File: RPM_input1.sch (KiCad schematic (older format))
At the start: 30 parts, among them P43 CONN_1, P44 CONN_1, P45 CONN_1, P46 CONN_1, P47 CONN_1, SW8 SWITCH_INV, U8 TL082CN, U9 LM1815

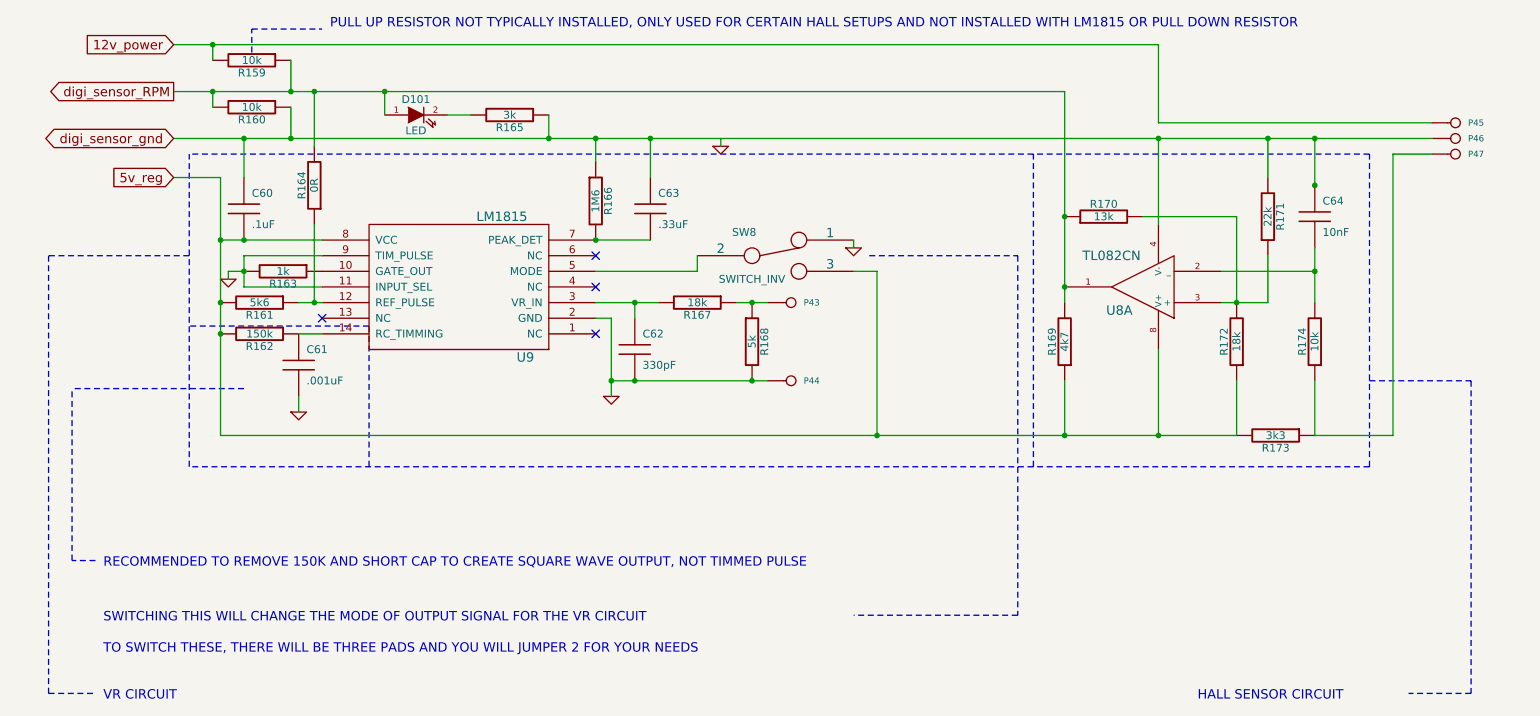
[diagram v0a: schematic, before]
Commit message: Removed LM1815 options. Now adaptive mode and square waves are the default,
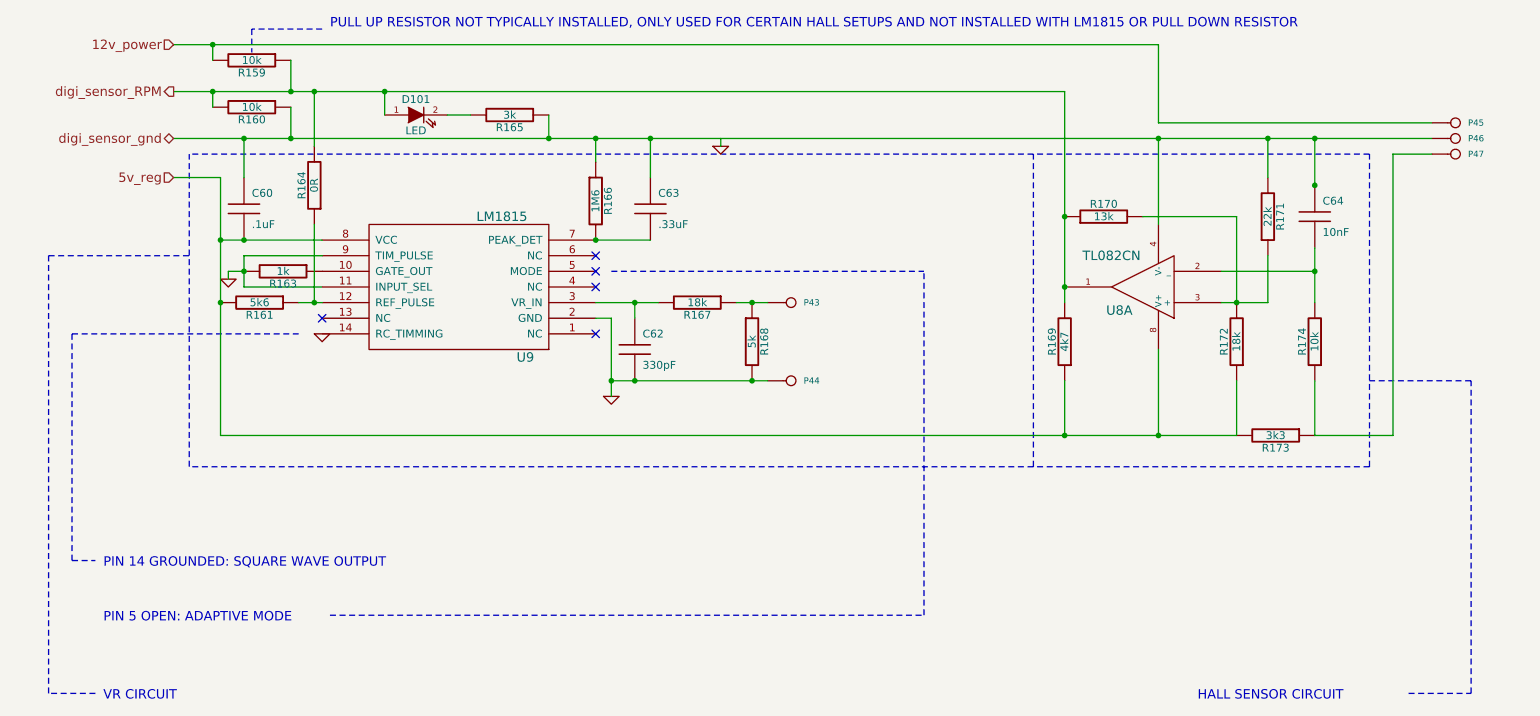
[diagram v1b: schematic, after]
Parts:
- removed C61: .001uF, C1V7, symbol C
- removed R162: 150k, R4-SM0805, symbol R
- removed SW8: SWITCH_INV, SIL-3, symbol SWITCH_INV
- C60: Field1 (none) -> newark,97M4164; Field2 (none) -> vendor1, smd w hem; Field3 (none) -> vendor2, thru w hem; Field4 (none) -> vendor2, smd w hem; Field5 (none) -> 50,V; Field6 (none) -> 20,%; Field7 (none) -> multilayer ceramic; Field8 (none) -> other,more,stuff
- C62: Field1 (none) -> newark,36K5919; Field2 (none) -> vendor1, smd w hem; Field3 (none) -> vendor2, thru w hem; Field4 (none) -> vendor2, smd w hem; Field5 (none) -> 100,V; Field6 (none) -> 5,%; Field7 (none) -> multilayered ceramic; Field8 (none) -> other,more,stuff
- C63: Field1 (none) -> newark,89F3212; Field2 (none) -> vendor1, smd w hem; Field3 (none) -> vendor2, thru w hem; Field4 (none) -> vendor2, smd w hem; Field5 (none) -> 50,V; Field6 (none) -> 20,%; Field7 (none) -> multilayer ceramic; Field8 (none) -> other,more,stuff
- C64: Field1 (none) -> newark,97M4158; Field2 (none) -> vendor1, smd w hem; Field3 (none) -> vendor2, thru w hem; Field4 (none) -> vendor2, smd w hem; Field5 (none) -> 10,V; Field6 (none) -> 10,%; Field7 (none) -> multilayer ceramic; Field8 (none) -> other,more,stuff
- D101: Field1 (none) -> newark,58k2469; Field2 (none) -> vendor1, smd w hem; Field3 (none) -> vendor2, thru w hem; Field4 (none) -> vendor2, smd w hem; Field5 (none) -> x,x; Field6 (none) -> x,x; Field7 (none) -> green; Field8 (none) -> other,more,stuff
- R159, R160: Field1 (none) -> newark,38k0328; Field2 (none) -> vendor1, smd w hem; Field3 (none) -> vendor2, thru w hem; Field4 (none) -> vendor2, smd w hem; Field5 (none) -> 250,mW; Field6 (none) -> 5,%; Field7 (none) -> carbon film; Field8 (none) -> other,more,stuff
- R161, R168: Field1 (none) -> newark,38K0382; Field2 (none) -> vendor1, smd w hem; Field3 (none) -> vendor2, thru w hem; Field4 (none) -> vendor2, smd w hem; Field5 (none) -> 250,mW; Field6 (none) -> 5,%; Field7 (none) -> carbon film; Field8 (none) -> other,more,stuff
- R163: Field1 (none) -> newark,38k0327; Field2 (none) -> vendor1, smd w hem; Field3 (none) -> vendor2, thru w hem; Field4 (none) -> vendor2, smd w hem; Field5 (none) -> 250,mW; Field6 (none) -> 5,%; Field7 (none) -> carbon film; Field8 (none) -> other,more,stuff
- R164: Field1 (none) -> vendor1, thru w hem; Field2 (none) -> vendor1, smd w hem; Field3 (none) -> vendor2, thru w hem; Field4 (none) -> vendor2, smd w hem; Field5 (none) -> power,W; Field6 (none) -> tol,%; Field7 (none) -> construct; Field8 (none) -> other,more,stuff
- R165: Field1 (none) -> newark,38k0340; Field2 (none) -> vendor1, smd w hem; Field3 (none) -> vendor2, thru w hem; Field4 (none) -> vendor2, smd w hem; Field5 (none) -> 1/4,W; Field6 (none) -> 5,%; Field7 (none) -> carbon film; Field8 (none) -> other,more,stuff
- R166: Field1 (none) -> newark,73K0277; Field2 (none) -> vendor1, smd w hem; Field3 (none) -> vendor2, thru w hem; Field4 (none) -> vendor2, smd w hem; Field5 (none) -> 250,mW; Field6 (none) -> 5,%; Field7 (none) -> carbon composition; Field8 (none) -> other,more,stuff
- R167: Field1 (none) -> newark,58K5022; Field2 (none) -> vendor1, smd w hem; Field3 (none) -> vendor2, thru w hem; Field4 (none) -> vendor2, smd w hem; Field5 (none) -> 250,mW; Field6 (none) -> 5,%; Field7 (none) -> carbon film; Field8 (none) -> other,more,stuff
- R169: Field1 (none) -> newark,58K3858; Field2 (none) -> vendor1, smd w hem; Field3 (none) -> vendor2, thru w hem; Field4 (none) -> vendor2, smd w hem; Field5 (none) -> 250,mW; Field6 (none) -> 1,%; Field7 (none) -> metal film; Field8 (none) -> other,more,stuff
- R170: Field1 (none) -> newark,94C4880; Field2 (none) -> vendor1, smd w hem; Field3 (none) -> vendor2, thru w hem; Field4 (none) -> vendor2, smd w hem; Field5 (none) -> 400,mW; Field6 (none) -> 1,%; Field7 (none) -> metal film; Field8 (none) -> other,more,stuff
- R171: Field1 (none) -> newark,71M1054; Field2 (none) -> vendor1, smd w hem; Field3 (none) -> vendor2, thru w hem; Field4 (none) -> vendor2, smd w hem; Field5 (none) -> 500,mW; Field6 (none) -> 1,%; Field7 (none) -> metal film; Field8 (none) -> other,more,stuff
- R172: Field1 (none) -> newark,58K3819; Field2 (none) -> vendor1, smd w hem; Field3 (none) -> vendor2, thru w hem; Field4 (none) -> vendor2, smd w hem; Field5 (none) -> 250,mW; Field6 (none) -> 1,%; Field7 (none) -> metal film; Field8 (none) -> other,more,stuff
- R173: Field1 (none) -> newark,58K3844; Field2 (none) -> vendor1, smd w hem; Field3 (none) -> vendor2, thru w hem; Field4 (none) -> vendor2, smd w hem; Field5 (none) -> 250,mW; Field6 (none) -> 1,%; Field7 (none) -> metal film; Field8 (none) -> other,more,stuff
- R174: Field1 (none) -> newark,58K3797; Field2 (none) -> vendor1, smd w hem; Field3 (none) -> vendor2, thru w hem; Field4 (none) -> vendor2, smd w hem; Field5 (none) -> 250,mW; Field6 (none) -> 1,%; Field7 (none) -> metal film; Field8 (none) -> other,more,stuff
- U8: Field1 (none) -> newark,89K1104; Field2 (none) -> vendor1, smd w hem; Field3 (none) -> digi,497-2213-5-ND; Field4 (none) -> vendor2, smd w hem; Field5 (none) -> x,x; Field6 (none) -> x,x; Field7 (none) -> opamp; Field8 (none) -> other,more,stuff
- U9: Field1 (none) -> newark,41K3517; Field2 (none) -> vendor2, thru e hem; Field3 (none) -> vendor2, thru w hem; Field4 (none) -> newark,41k3517; Field5 (none) -> x,x; Field6 (none) -> x,x; Field7 (none) -> VR RPM chip; Field8 (none) -> x,x,x
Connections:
- net GND: now also U9.14 (RC_TIMMING)
- no-connect marks 4 -> 5
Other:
- note added: "PIN 14 GROUNDED: SQUARE WAVE OUTPUT"
- note added: "PIN 5 OPEN: ADAPTIVE MODE"
- note removed: "RECOMMENDED TO REMOVE 150K AND SHORT CAP TO CREATE SQUARE WAVE OUTPUT, NOT TIMMED PULSE"
- note removed: "SWITCHING THIS WILL CHANGE THE MODE OF OUTPUT SIGNAL FOR THE VR CIRCUIT"
- note removed: "TO SWITCH THESE, THERE WILL BE THREE PADS AND YOU WILL JUMPER 2 FOR YOUR NEEDS"

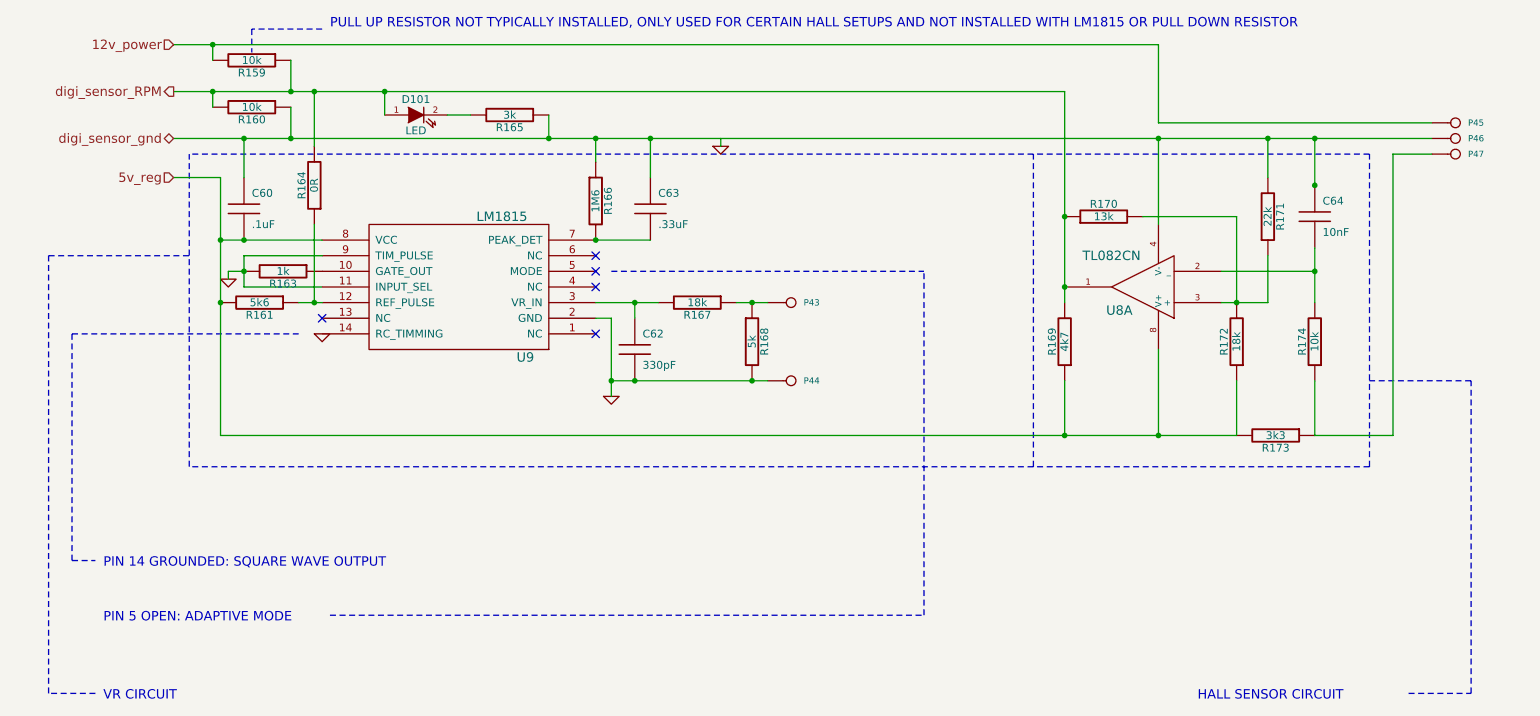
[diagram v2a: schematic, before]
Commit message: Implemented P&H, removed current sense circuitry, removed all unnecessary files from the repo
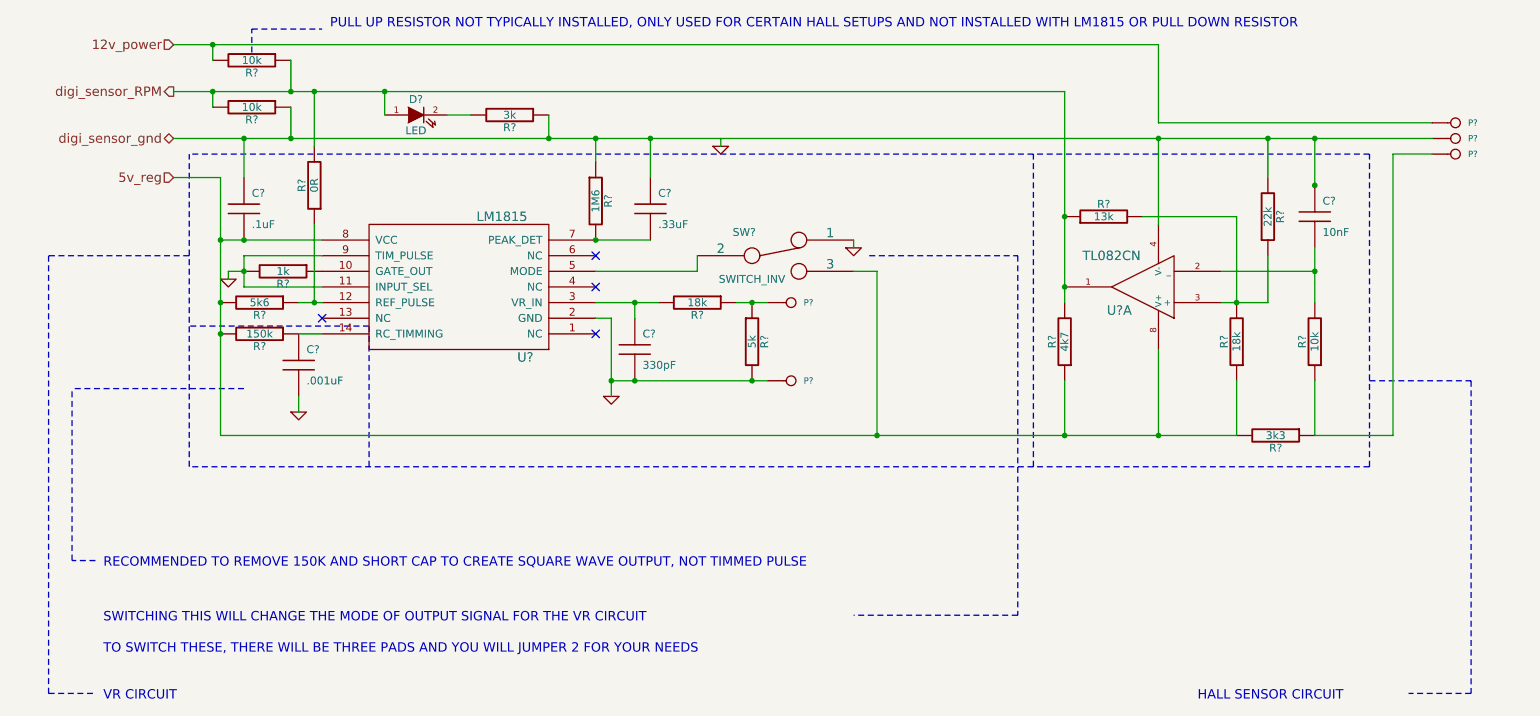
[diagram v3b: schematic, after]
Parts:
- added C?: .001uF, C1V7, symbol C
- added R?: 150k, R4-SM0805, symbol R
- added SW?: SWITCH_INV, SIL-3, symbol SWITCH_INV
- U?: renamed from U9; Field7 VR RPM chip -> x
- U?: renamed from U8; Field7 opamp -> x
- renumbered C63 to C?, C60 to C?, C62 to C?, C64 to C?, D101 to D?, P43 to P?, P44 to P?, P46 to P?, P47 to P?, P45 to P?, R161 to R?, R163 to R?, R167 to R?, R166 to R?, R160 to R?, R165 to R?, R164 to R?, R159 to R?, R168 to R?, R173 to R?, R172 to R?, R174 to R?, R171 to R?, R170 to R?, R169 to R?
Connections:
- net 5v_reg: now also R?.2, SW?.3
- net GND: now also C?.2, SW?.1; no longer U?.14 (RC_TIMMING)
- net at U?.5 (MODE): now also SW?.2
- new net: C?.1, R?.1, U?.14 (RC_TIMMING)
- no-connect marks 5 -> 4
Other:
- note added: "RECOMMENDED TO REMOVE 150K AND SHORT CAP TO CREATE SQUARE WAVE OUTPUT, NOT TIMMED PULSE"
- note added: "SWITCHING THIS WILL CHANGE THE MODE OF OUTPUT SIGNAL FOR THE VR CIRCUIT"
- note added: "TO SWITCH THESE, THERE WILL BE THREE PADS AND YOU WILL JUMPER 2 FOR YOUR NEEDS"
- note removed: "PIN 14 GROUNDED: SQUARE WAVE OUTPUT"
- note removed: "PIN 5 OPEN: ADAPTIVE MODE"
